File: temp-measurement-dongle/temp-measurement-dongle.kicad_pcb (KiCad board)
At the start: 2 copper layers, 57.1 x 46.3 mm, 41 parts, among them J1 1.47 IPS LCD, J2 USB2UART, Q1 SS8050, Q2 SS8050, SW1 RST, SW2 Boot, SW3 IN1, SW4 IN2, SW5 IN4, SW6 IN4, U1 ESP32-S3-WROOM-1, U2 CH340C, U4 AMS1117-3.3

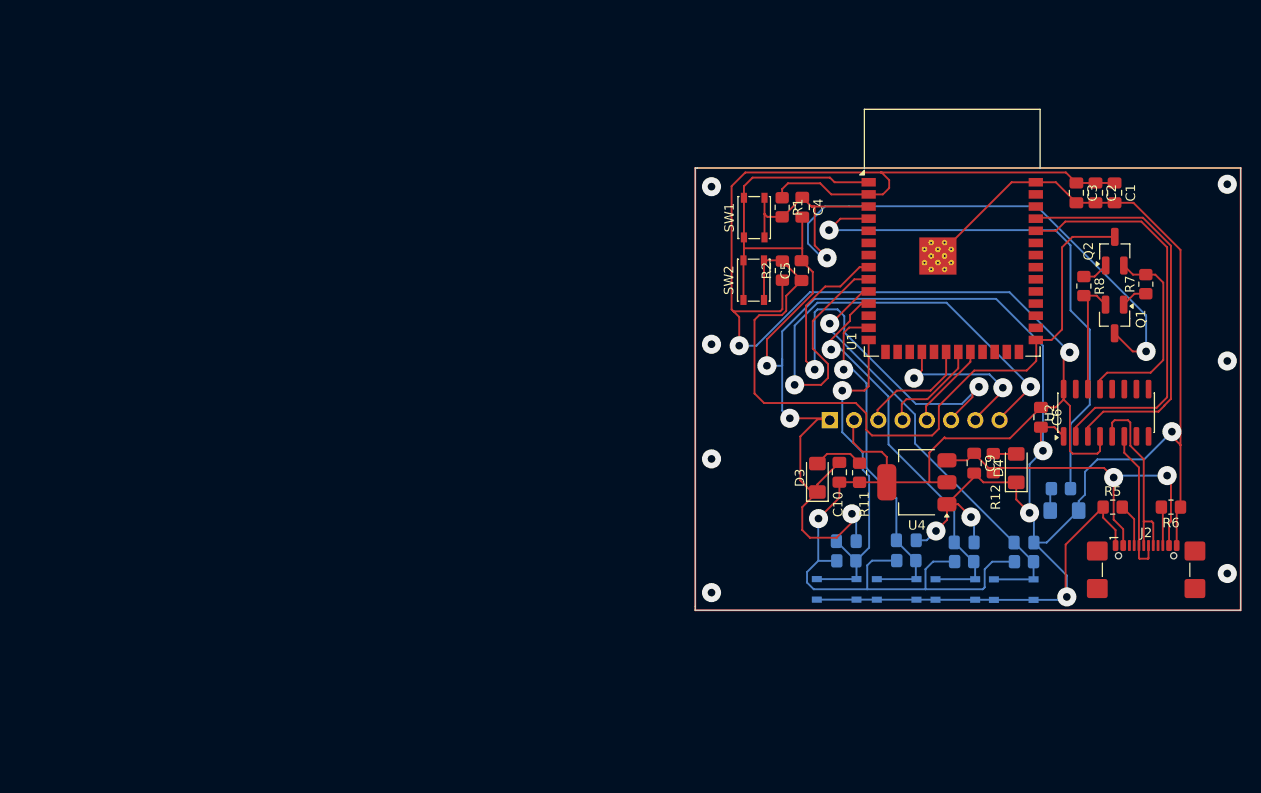
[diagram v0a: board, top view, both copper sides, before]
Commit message: feat: finish schematic of temperature-measurement-dongle
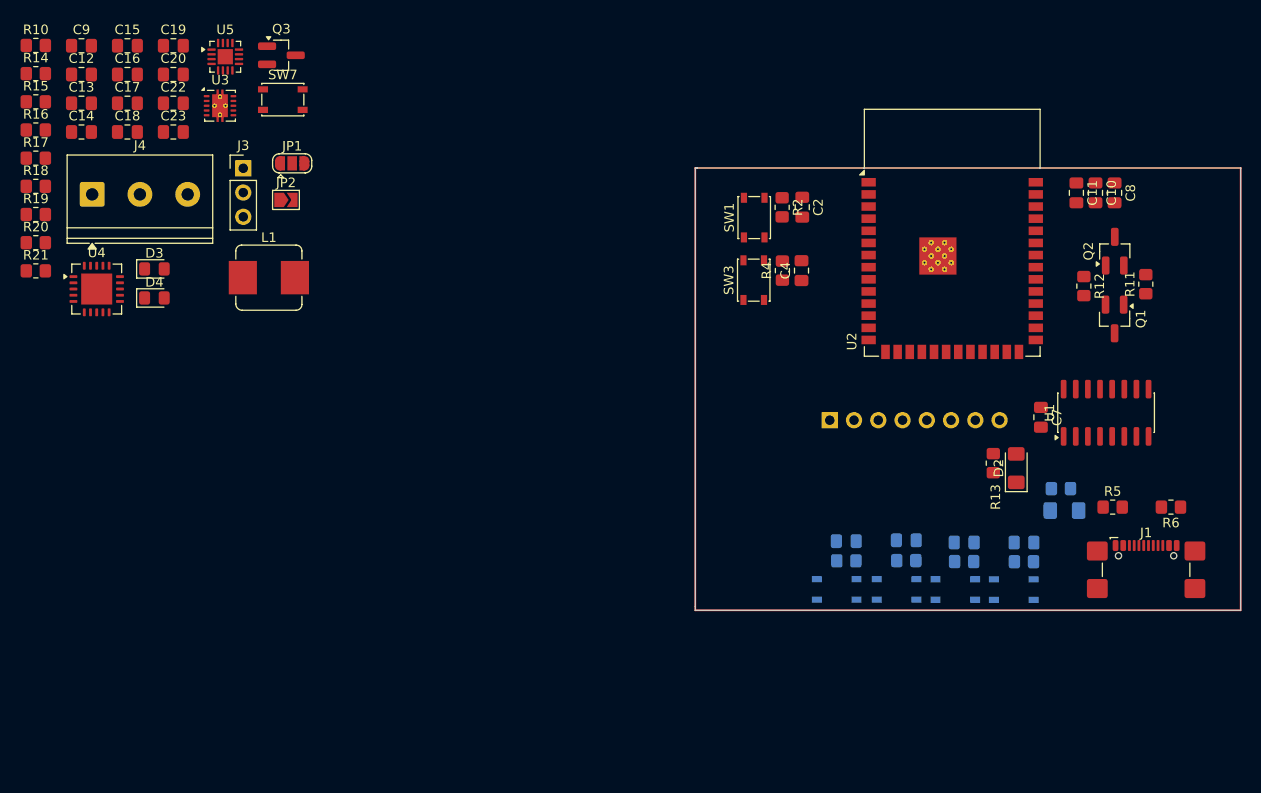
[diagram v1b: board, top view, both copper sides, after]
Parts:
- removed the C10 at (129.9, 103.7)
- removed the R11 at (132.0, 103.7)
- added C12: 100nF, Capacitor_SMD:C_0805_2012Metric_Pad1.18x1.45mm_HandSolder, F.Cu at (50.5, 62.0)
- added C13: 10uF, Capacitor_SMD:C_0805_2012Metric_Pad1.18x1.45mm_HandSolder, F.Cu at (50.5, 65.0)
- added C14: 0.1uF, Capacitor_SMD:C_0805_2012Metric_Pad1.18x1.45mm_HandSolder, F.Cu at (50.5, 68.0)
- added C15: 1uF, Capacitor_SMD:C_0805_2012Metric_Pad1.18x1.45mm_HandSolder, F.Cu at (55.3, 59.0)
- added C16: 10uF, Capacitor_SMD:C_0805_2012Metric_Pad1.18x1.45mm_HandSolder, F.Cu at (55.3, 62.0)
- added C17: 10uF, Capacitor_SMD:C_0805_2012Metric_Pad1.18x1.45mm_HandSolder, F.Cu at (55.3, 65.0)
- added C18: 100nF, Capacitor_SMD:C_0805_2012Metric_Pad1.18x1.45mm_HandSolder, F.Cu at (55.3, 68.0)
- added C19: 100nF, Capacitor_SMD:C_0805_2012Metric_Pad1.18x1.45mm_HandSolder, F.Cu at (60.2, 59.0)
- added C20: 100nF, Capacitor_SMD:C_0805_2012Metric_Pad1.18x1.45mm_HandSolder, F.Cu at (60.2, 62.0)
- added C22: 4.7uF, Capacitor_SMD:C_0805_2012Metric_Pad1.18x1.45mm_HandSolder, F.Cu at (60.2, 65.0)
- added C23: 4.7uF, Capacitor_SMD:C_0805_2012Metric_Pad1.18x1.45mm_HandSolder, F.Cu at (60.2, 68.0)
- added D4: red, LED_SMD:LED_0805_2012Metric_Pad1.15x1.40mm_HandSolder, F.Cu at (58.2, 85.4)
- added J3: ConnBattery, Connector_PinHeader_2.54mm:PinHeader_1x03_P2.54mm_Vertical, F.Cu at (67.5, 71.8)
- added J4: RTD_PT100, TerminalBlock_Phoenix:TerminalBlock_Phoenix_PT-1,5-3-5.0-H_1x03_P5.00mm_Horizontal, F.Cu at (51.7, 74.6)
- added JP1: 3_OR_2_Wire, Jumper:SolderJumper-3_P1.3mm_Open_RoundedPad1.0x1.5mm, F.Cu at (72.6, 71.3)
- added JP2: 2_Wire, Jumper:SolderJumper-2_P1.3mm_Open_TrianglePad1.0x1.5mm, F.Cu at (71.9, 75.1)
- added L1: 22uH 1A, Inductor_SMD:L_Bourns_SRP7028A_7.3x6.6mm, F.Cu at (70.2, 83.3)
- added Q3: SS8050, Package_TO_SOT_SMD:SOT-23_Handsoldering, F.Cu at (71.5, 60.0)
- added R10: 1k, Resistor_SMD:R_0805_2012Metric_Pad1.20x1.40mm_HandSolder, F.Cu at (45.8, 59.0)
- added R14: 1k, Resistor_SMD:R_0805_2012Metric_Pad1.20x1.40mm_HandSolder, F.Cu at (45.8, 61.9)
- added R15: 100, Resistor_SMD:R_0805_2012Metric_Pad1.20x1.40mm_HandSolder, F.Cu at (45.8, 64.9)
- added R16: 46.4K, Resistor_SMD:R_0805_2012Metric_Pad1.20x1.40mm_HandSolder, F.Cu at (45.8, 67.8)
- added R17: 2K2, Resistor_SMD:R_0805_2012Metric_Pad1.20x1.40mm_HandSolder, F.Cu at (45.8, 70.8)
- added R18: 1.13k, Resistor_SMD:R_0805_2012Metric_Pad1.20x1.40mm_HandSolder, F.Cu at (45.8, 73.7)
- added R19: 400 1%, Resistor_SMD:R_0805_2012Metric_Pad1.20x1.40mm_HandSolder, F.Cu at (45.8, 76.7)
- added R20: 1K5, Resistor_SMD:R_0805_2012Metric_Pad1.20x1.40mm_HandSolder, F.Cu at (45.8, 79.6)
- added R21: 1K5, Resistor_SMD:R_0805_2012Metric_Pad1.20x1.40mm_HandSolder, F.Cu at (45.8, 82.6)
- added SW7: IN5, Button_Switch_SMD:SW_SPST_PTS810, F.Cu at (71.6, 64.6)
- added U3: TPS63001_SEPIC_3V3, Package_SON:Texas_DRC0010J_ThermalVias, F.Cu at (65.0, 65.3)
- added U5: BQ24075RGT_DPPM, Package_DFN_QFN:VQFN-16-1EP_3x3mm_P0.5mm_EP1.6x1.6mm, F.Cu at (65.6, 60.1)
- C9: value 22uF -> 100nF
- D2: renamed from D4; value TXD -> VDD
- D3: value TXD -> green; footprint LED_SMD:LED_1206_3216Metric_Pad1.42x1.75mm_HandSolder -> LED_SMD:LED_0805_2012Metric_Pad1.15x1.40mm_HandSolder
- U4: value AMS1117-3.3 -> MAX31865xTP; footprint Package_TO_SOT_SMD:SOT-223-3_TabPin2 -> Package_DFN_QFN:TQFN-20-1EP_5x5mm_P0.65mm_EP3.25x3.25mm
- moved C9 103.2 mm to (50.5, 59.0), turned to 0 degrees
- moved U4 88.2 mm to (52.1, 84.5), turned to 0 degrees
- moved D3 72.8 mm to (58.2, 82.4), turned to 0 degrees
- renumbered C7 to C1, C2 to C10, C3 to C11, C4 to C2, C8 to C3, C5 to C4, C11 to C5, C12 to C6, C6 to C7, C1 to C8, D5 to D1, J2 to J1, J1 to J2, R4 to R1, R7 to R11, R8 to R12, R12 to R13, R1 to R2, R9 to R3, R2 to R4, R10 to R7, R3 to R8, R13 to R9, SW3 to SW2, SW2 to SW3, U2 to U1, U1 to U2
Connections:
- C9 pad 1: +5V -> /IN5
- D1 pad 2: Net-(D5-A) -> Net-(D1-A)
- D3 pad 1: GND -> /~{PGOOD}
- J1 pad A4: +5V -> VBUS
- J1 pad A9: +5V -> VBUS
- J1 pad B4: +5V -> VBUS
- J1 pad B9: +5V -> VBUS
- J2 pad 3: /SCL -> /SCK
- J2 pad 4: /SDA -> /MOSI
- R13 pad 1: +5V -> VDD
- R8 pad 1: Net-(U1-IO4) -> Net-(D1-A)
- R8 pad 2: Net-(D5-A) -> Net-(U2-IO4)
- U2 pad 12: unconnected-(U1-IO8-Pad12) -> /MAX31865DRDY
- U2 pad 17: unconnected-(U1-IO9-Pad17) -> /MAX31865CS
- U2 pad 19: unconnected-(U1-IO11-Pad19) -> /MOSI
- U2 pad 20: /SCL -> /SCK
- U2 pad 21: /SDA -> /MISO
- U2 pad 23: unconnected-(U1-IO21-Pad23) -> /IN5
- U2 pad 31: unconnected-(U1-IO38-Pad31) -> Net-(Q3-E)
- U2 pad 4: Net-(U1-IO4) -> Net-(U2-IO4)
- U4 pad 1: GND -> Net-(U4-BIAS)
- U4 pad 2: +3.3V -> Net-(U4-BIAS)
- U4 pad 3: +5V -> Net-(U4-ISENSOR)
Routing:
- net GND: track 312.0 -> 0.00 mm, vias 9 -> 0
- net +3.3V: track 226.3 -> 0.00 mm, vias 3 -> 0
- net /IO0: track 81.2 -> 0.00 mm
- net /EN: track 76.1 -> 0.00 mm, vias 2 -> 0
- net /BLK: track 58.4 -> 0.00 mm, vias 2 -> 0
- net Net-(U1-IO4): track 57.7 -> 0.00 mm, vias 1 -> 0
- net /DC: track 49.1 -> 0.00 mm, vias 2 -> 0
- net /IN1: track 46.1 -> 0.00 mm, vias 1 -> 0
- net /RXD0: track 42.8 -> 0.00 mm
- net /TXD0: track 42.4 -> 0.00 mm
- net /IN2: track 42.1 -> 0.00 mm, vias 1 -> 0
- net +5V: track 40.0 -> 0.00 mm, vias 2 -> 0
- net /IN3: track 36.5 -> 0.00 mm, vias 1 -> 0
- net /IN4: track 36.4 -> 0.00 mm, vias 1 -> 0
- net /DTR: track 21.4 -> 0.00 mm
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
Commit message: feat: finish 2 layer routing temperature measurement dongle
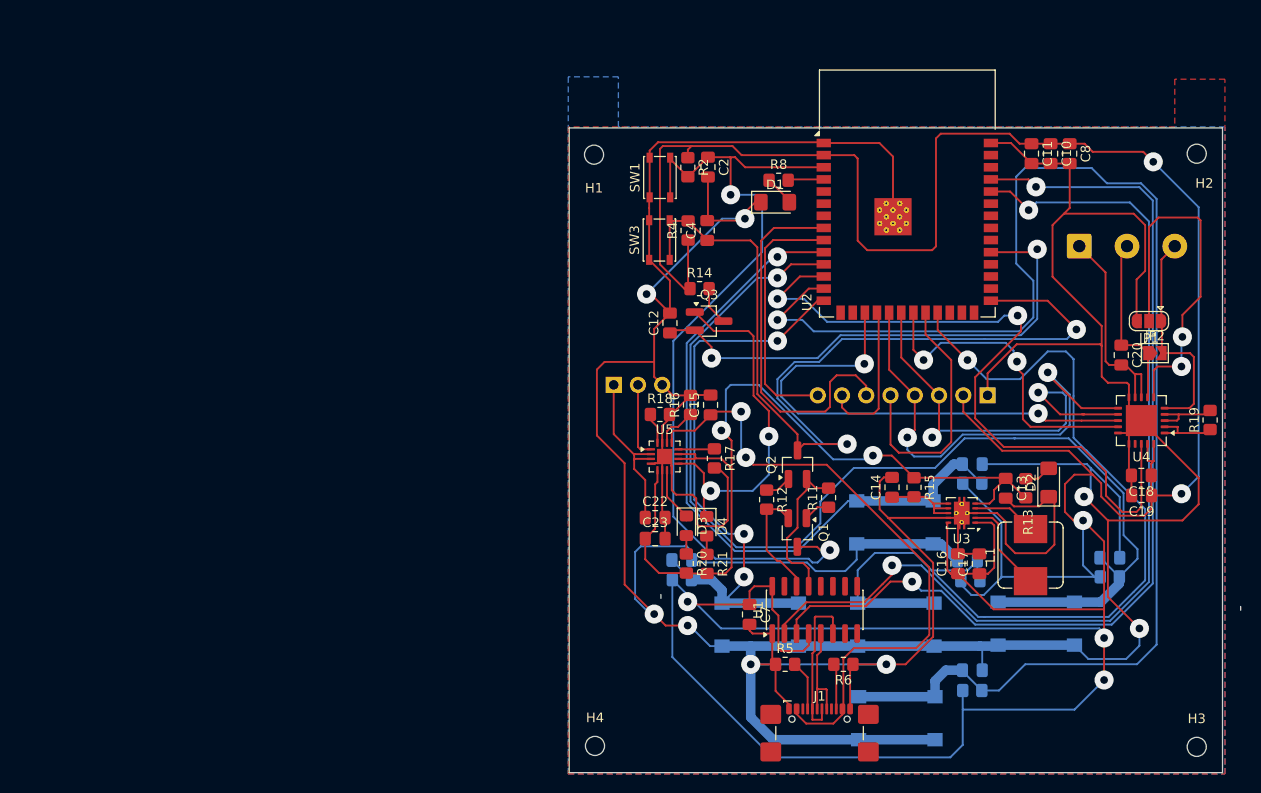
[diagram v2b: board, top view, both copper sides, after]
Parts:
- added H1: MountingHole, MountingHole:MountingHole_2mm, F.Cu at (104.2, 70.4)
- added H2: MountingHole, MountingHole:MountingHole_2mm, F.Cu at (167.3, 70.3)
- added H3: MountingHole, MountingHole:MountingHole_2mm, F.Cu at (167.3, 132.4)
- added H4: MountingHole, MountingHole:MountingHole_2mm, F.Cu at (104.3, 132.3)
- C9, J3, J4, R10: moved to B.Cu
- D1: value TXD -> INDICATOR; moved to F.Cu
- R8: moved to F.Cu
- SW2, SW4, SW5, SW6: footprint Button_Switch_SMD:SW_SPST_PTS810 -> Button_Switch_SMD:SW_SPST_Omron_B3FS-100xP
- SW7: footprint Button_Switch_SMD:SW_SPST_PTS810 -> Button_Switch_SMD:SW_SPST_Omron_B3FS-100xP; moved to B.Cu
- moved R19 124.8 mm to (168.7, 98.2), turned to 90 degrees
- moved R10 112.8 mm to (143.6, 115.0)
- moved C18 112.1 mm to (161.5, 104.0), turned to 180 degrees
- moved C19 111.8 mm to (161.5, 106.1), turned to 180 degrees
- moved U4 110.2 mm to (161.5, 98.2), turned to 180 degrees
- moved C9 107.3 mm to (143.3, 112.9), turned to 180 degrees
- moved C13 104.8 mm to (147.3, 105.3), turned to -90 degrees
- moved C20 103.5 mm to (159.4, 91.4), turned to -90 degrees
- moved J4 103.5 mm to (155.0, 80.0)
- moved C17 101.4 mm to (144.6, 113.2), turned to 90 degrees
- moved C16 100.9 mm to (142.3, 113.2), turned to 90 degrees
- moved R15 100.4 mm to (137.7, 105.2), turned to -90 degrees
- moved C14 92.7 mm to (135.4, 105.2), turned to 90 degrees
- moved JP2 92.4 mm to (162.9, 91.2)
- moved JP1 91.2 mm to (162.3, 87.8), turned to 180 degrees
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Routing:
- net GND: track 0.00 -> 547.2 mm, vias 0 -> 8
- net +3.3V: track 0.00 -> 404.6 mm, vias 0 -> 6
- net /IN3: track 0.00 -> 148.9 mm, vias 0 -> 1
- net /IN2: track 0.00 -> 116.9 mm, vias 0 -> 1
- net /RXD0: track 0.00 -> 102.6 mm, vias 0 -> 2
- net /TXD0: track 0.00 -> 102.0 mm, vias 0 -> 2
- net /IN5: track 0.00 -> 100.2 mm, vias 0 -> 1
- net /IO0: track 0.00 -> 97.9 mm, vias 0 -> 2
- net /EN: track 0.00 -> 89.3 mm, vias 0 -> 2
- net VDD: track 0.00 -> 88.9 mm, vias 0 -> 2
- net /MAX31865DRDY: track 0.00 -> 74.9 mm, vias 0 -> 2
- net /IN1: track 0.00 -> 73.6 mm, vias 0 -> 1
- net VBUS: track 0.00 -> 67.4 mm, vias 0 -> 2
- net /IN4: track 0.00 -> 62.4 mm, vias 0 -> 3
- net Net-(Q3-E): track 0.00 -> 54.4 mm, vias 0 -> 2
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- added copper zone on B.Cu, net (none)
- added copper zone on F.Cu, net (none)
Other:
- board size 57.1 x 46.3 mm -> 70.3 x 67.5 mm
